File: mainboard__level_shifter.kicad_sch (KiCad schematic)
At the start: 66 parts

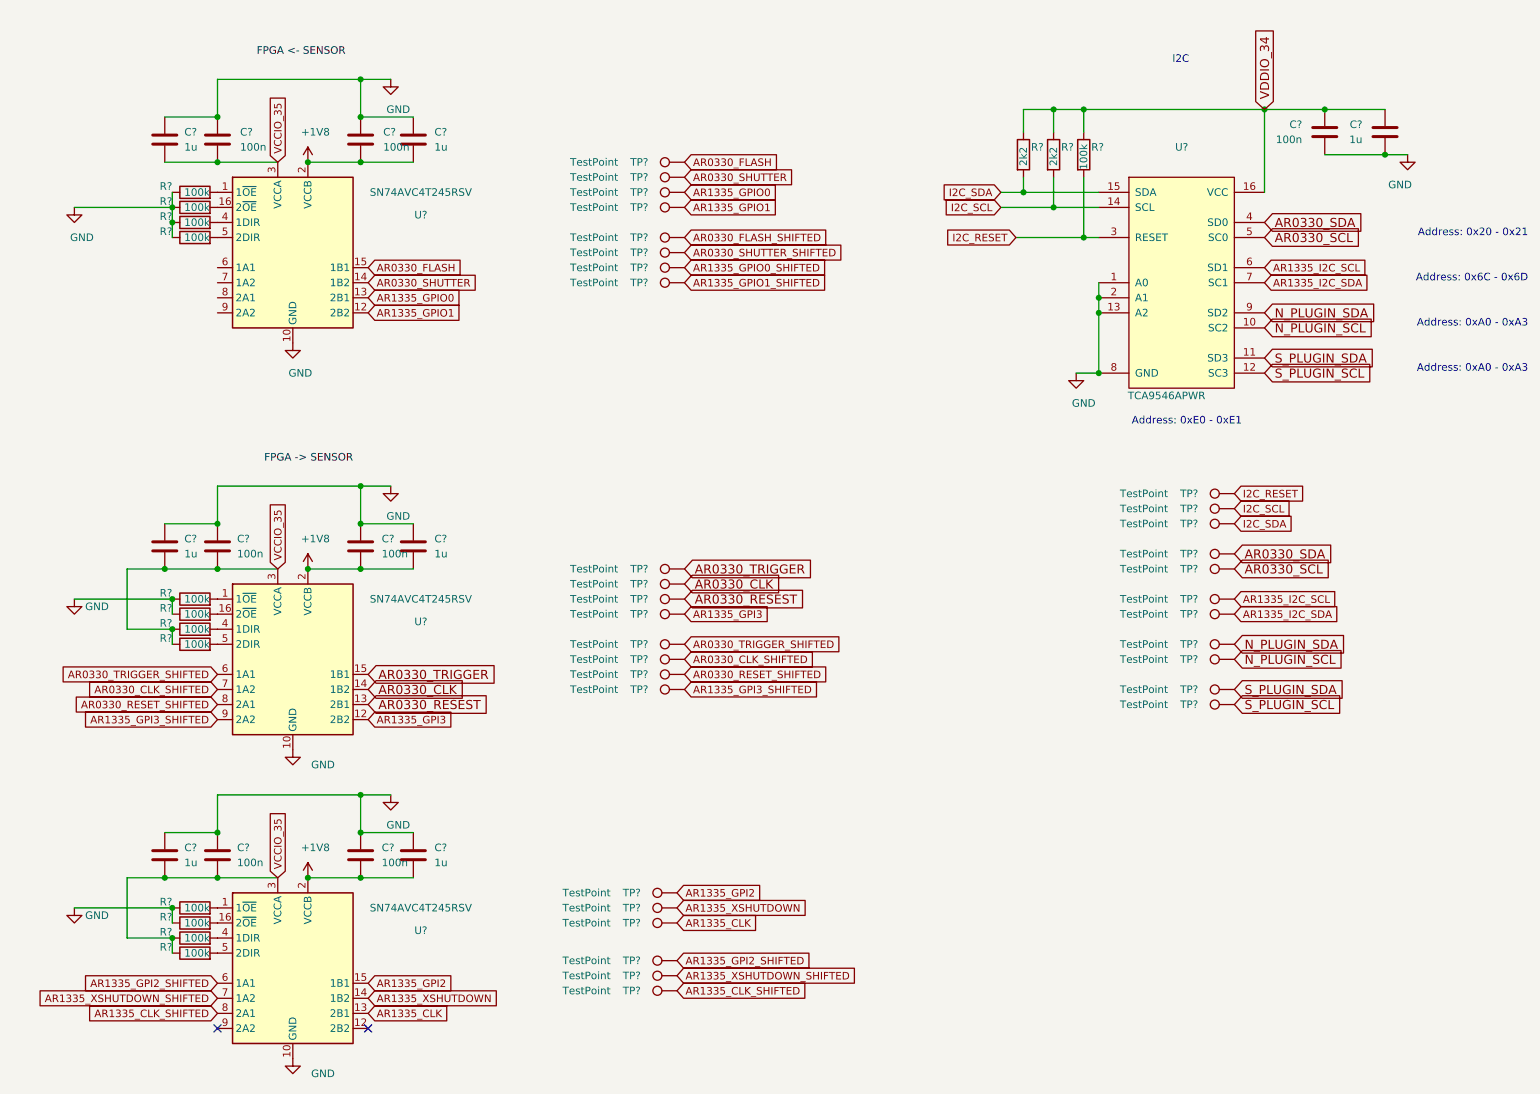
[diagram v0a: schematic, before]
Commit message: small tweaks; add mipi termination
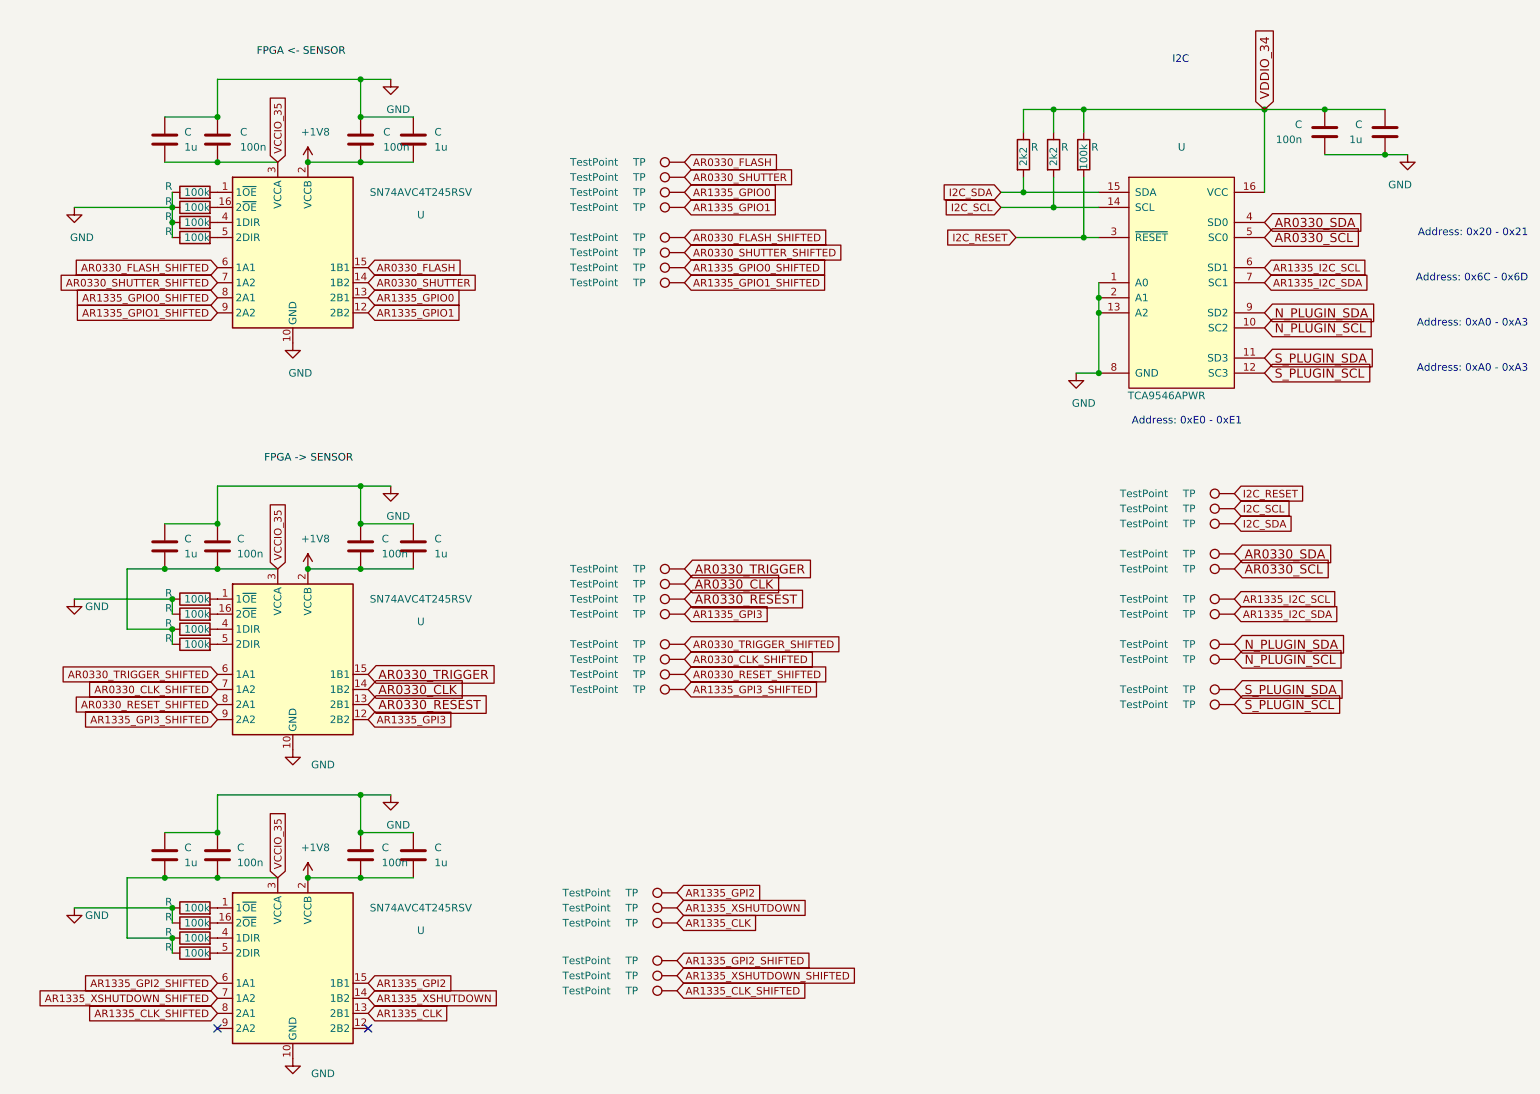
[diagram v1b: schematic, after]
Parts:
- gave numbers to parts that had none: 4
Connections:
- net AR0330_FLASH_SHIFTED: now also U.6 (1A1)
- net AR0330_SHUTTER_SHIFTED: now also U.7 (1A2)
- net AR1335_GPIO0_SHIFTED: now also U.8 (2A1)
- net AR1335_GPIO1_SHIFTED: now also U.9 (2A2)
